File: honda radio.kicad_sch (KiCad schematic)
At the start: 77 parts, among them J1 DE9_Receptacle_MountingHoles, J2 DE9_Receptacle_MountingHoles, J3 DB25_Receptacle_MountingHoles, J4 RCA Jack, J5 SJ-3523-SMT-TR, J6 Arduino Nano Every, J7 Adafruit MPM3610, J8 TinySine AudioB Plus V3r2, K1 G6L-1F-TR_DC5, K10 G6L-1F-TR_DC5, K11 G6L-1F-TR_DC5, K12 G6L-1F-TR_DC5, K2 G6L-1F-TR_DC5, K3 G6L-1F-TR_DC5, K4 G6L-1F-TR_DC5, K5 G6L-1F-TR_DC5, K6 G6L-1F-TR_DC5, K7 G6L-1F-TR_DC5, K8 G6L-1F-TR_DC5, K9 G2RL-2A-DC5, Q1 BC547, Q10 BC547, Q11 BC547, Q12 BC547, Q2 BC547, Q3 BC547, Q4 BC547, Q5 BC547, Q6 BC547, Q7 BC547, Q8 BC547, Q9 BC547

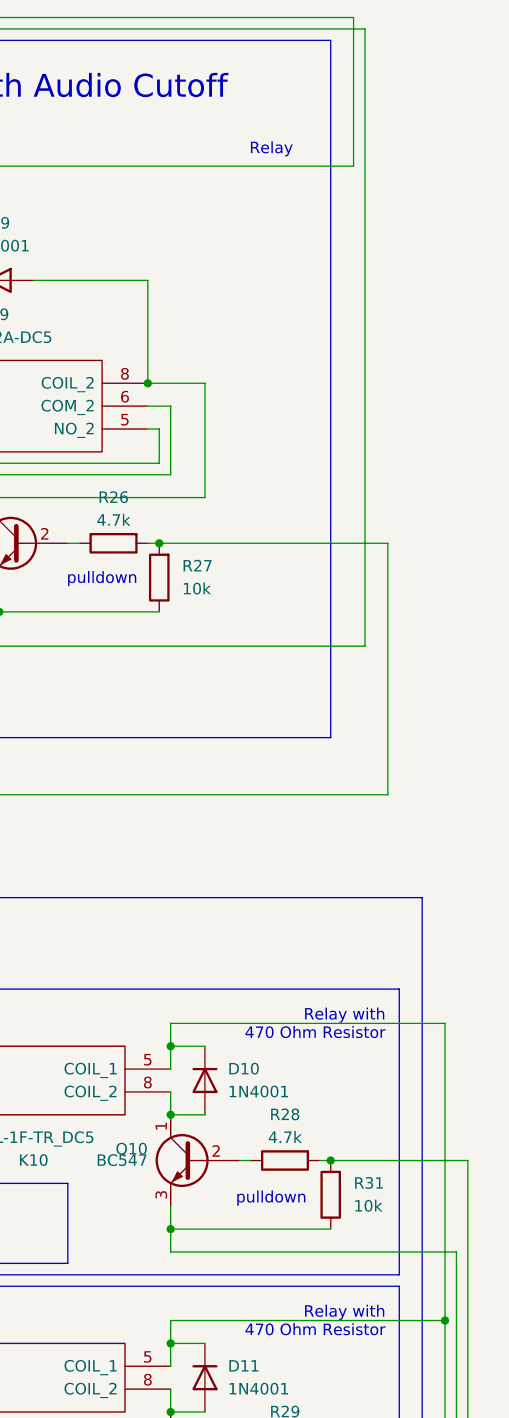
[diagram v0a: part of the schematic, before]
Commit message: added missing trace
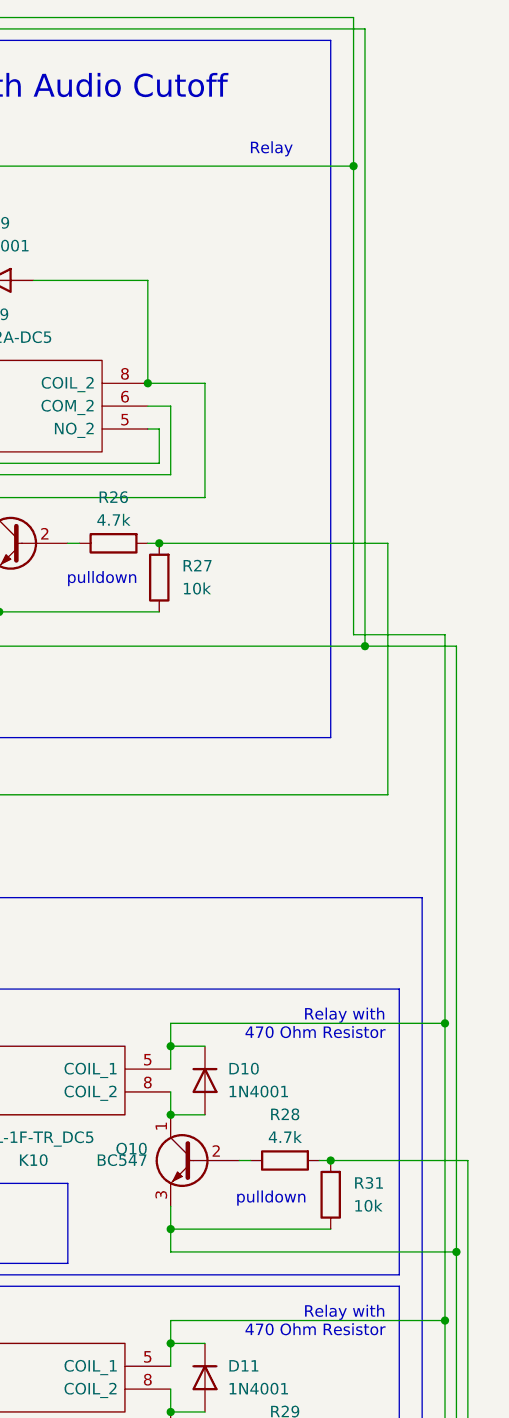
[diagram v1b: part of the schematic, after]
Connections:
- net at D1.1 (K), D2.1 (K), D3.1 (K)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: now also D10.1 (K), D11.1 (K), D12.1 (K), D6.1 (K), D7.1 (K), D8.1 (K), K10.5 (COIL_1), K11.5 (COIL_1), K12.5 (COIL_1), K6.5 (COIL_1), K7.5 (COIL_1), K8.5 (COIL_1)
- net at Q10.3 (E), Q11.3 (E), Q12.3 (E)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: now also J1.0 (PAD), J1.9 (GND), J2.0 (PAD), J2.1 (1.8V_TRIG), J3.0 (PAD), J3.1 (GND), J3.14 (GND), J4.1 (GND), J4.3 (GND), J5.1 (SLEEVE), J6.19 (GND), J6.2 (GND), J7.1 (GND), J8.1 (GND), J8.16 (GND), J8.6 (GND), Q1.3 (E), Q2.3 (E), Q3.3 (E), Q4.3 (E), Q5.3 (E), Q9.3 (E), R15.1, R16.1, R27.1, R4.1, R5.1, R6.1
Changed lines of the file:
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@@
 	)
 	(junction
+		(at 389.89 63.5)
+		(diameter 0)
+		(color 0 0 0 0)
+	)
+	(junction
 		(at 327.66 250.19)
 		(diameter 0)
@@
 	)
 	(junction
+		(at 391.16 116.84)
+		(diameter 0)
+		(color 0 0 0 0)
+	)
+	(junction
 		(at 303.53 207.01)
 		(diameter 0)
@@
 	)
 	(junction
+		(at 400.05 158.75)
+		(diameter 0)
+		(color 0 0 0 0)
+	)
+	(junction
 		(at 401.32 250.19)
 		(diameter 0)
@@
 	)
 	(junction
+		(at 401.32 184.15)
+		(diameter 0)
+		(color 0 0 0 0)
+	)
+	(junction
 		(at 285.75 234.95)
 		(diameter 0)
@@
 	(wire
 		(pts
+			(xy 389.89 115.57) (xy 389.89 63.5)
+		)
+		(stroke
+			(width 0.381)
+			(type default)
+			(color 255 0 0 1)
+		)
+	)
+	(wire
+		(pts
 			(xy 52.07 92.71) (xy 133.35 92.71)
 		)
@@
 	(wire
 		(pts
+			(xy 400.05 158.75) (xy 400.05 115.57)
+		)
+		(stroke
+			(width 0.381)
+			(type default)
+			(color 255 0 0 1)
+		)
+	)
+	(wire
+		(pts
 			(xy 44.45 111.76) (xy 55.88 111.76)
 		)
@@
 	(wire
 		(pts
+			(xy 391.16 116.84) (xy 401.32 116.84)
+		)
+		(stroke
+			(width 0.381)
+			(type default)
+			(color 0 0 0 1)
+		)
+	)
+	(wire
+		(pts
 			(xy 53.34 43.18) (xy 241.3 43.18)
 		)
@@
 	(wire
 		(pts
+			(xy 401.32 116.84) (xy 401.32 184.15)
+		)
+		(stroke
+			(width 0.381)
+			(type default)
+			(color 0 0 0 1)
+		)
+	)
+	(wire
+		(pts
 			(xy 147.32 101.6) (xy 147.32 179.07)
 		)
@@
 		)
 	)
+	(wire
+		(pts
+			(xy 400.05 115.57) (xy 389.89 115.57)
+		)
+		(stroke
+			(width 0.381)
+			(type default)
+			(color 255 0 0 1)
+		)
+	)
